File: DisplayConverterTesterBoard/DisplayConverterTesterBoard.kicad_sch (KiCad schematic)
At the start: 1 part

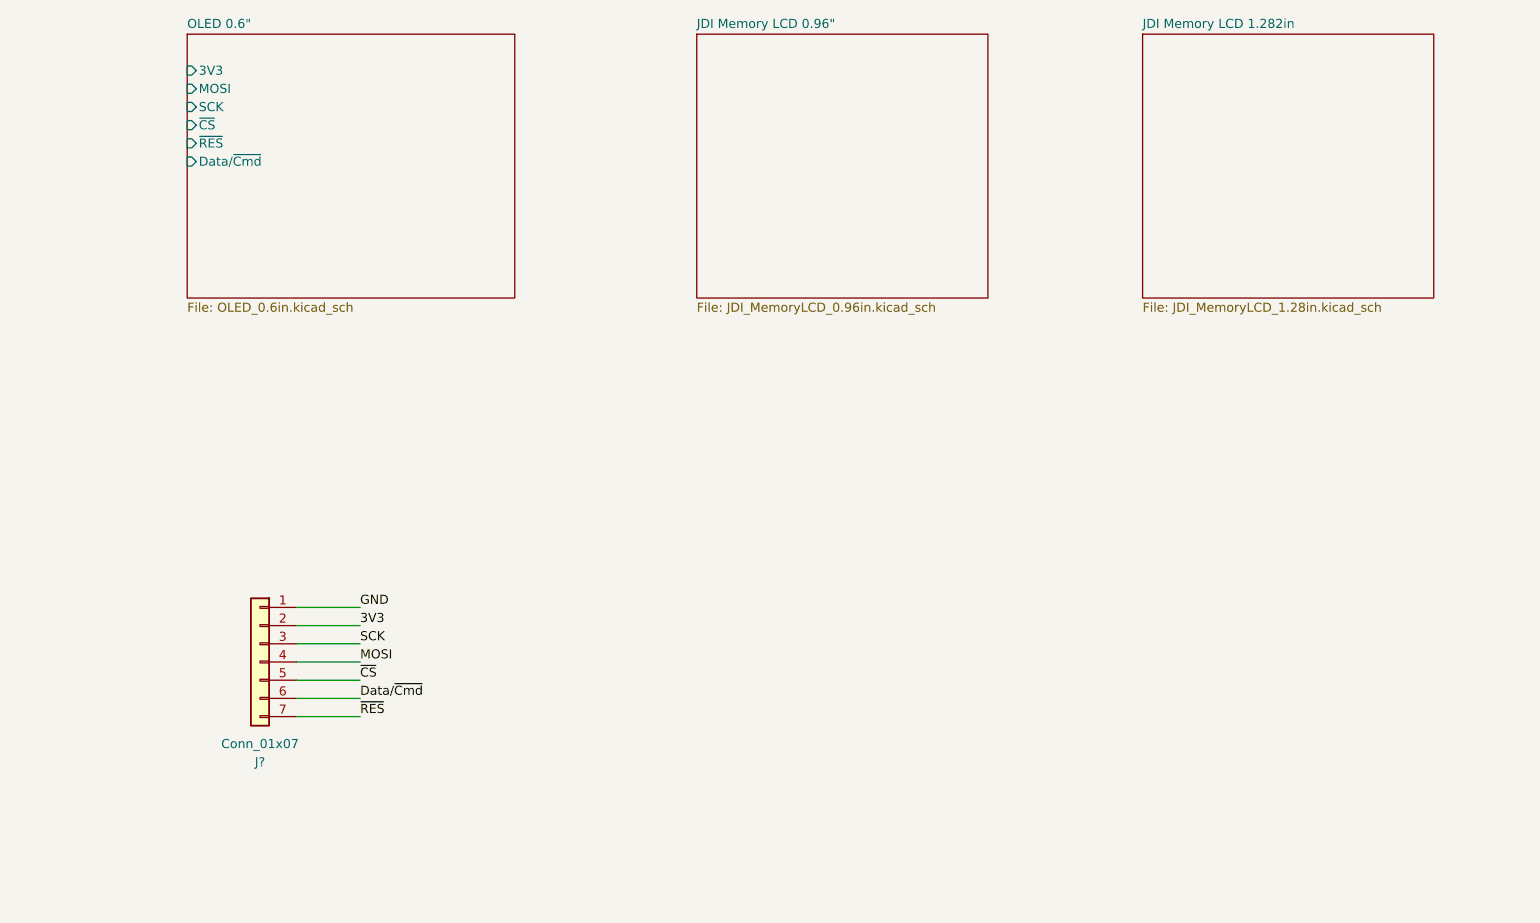
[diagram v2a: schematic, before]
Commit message: fix pinout
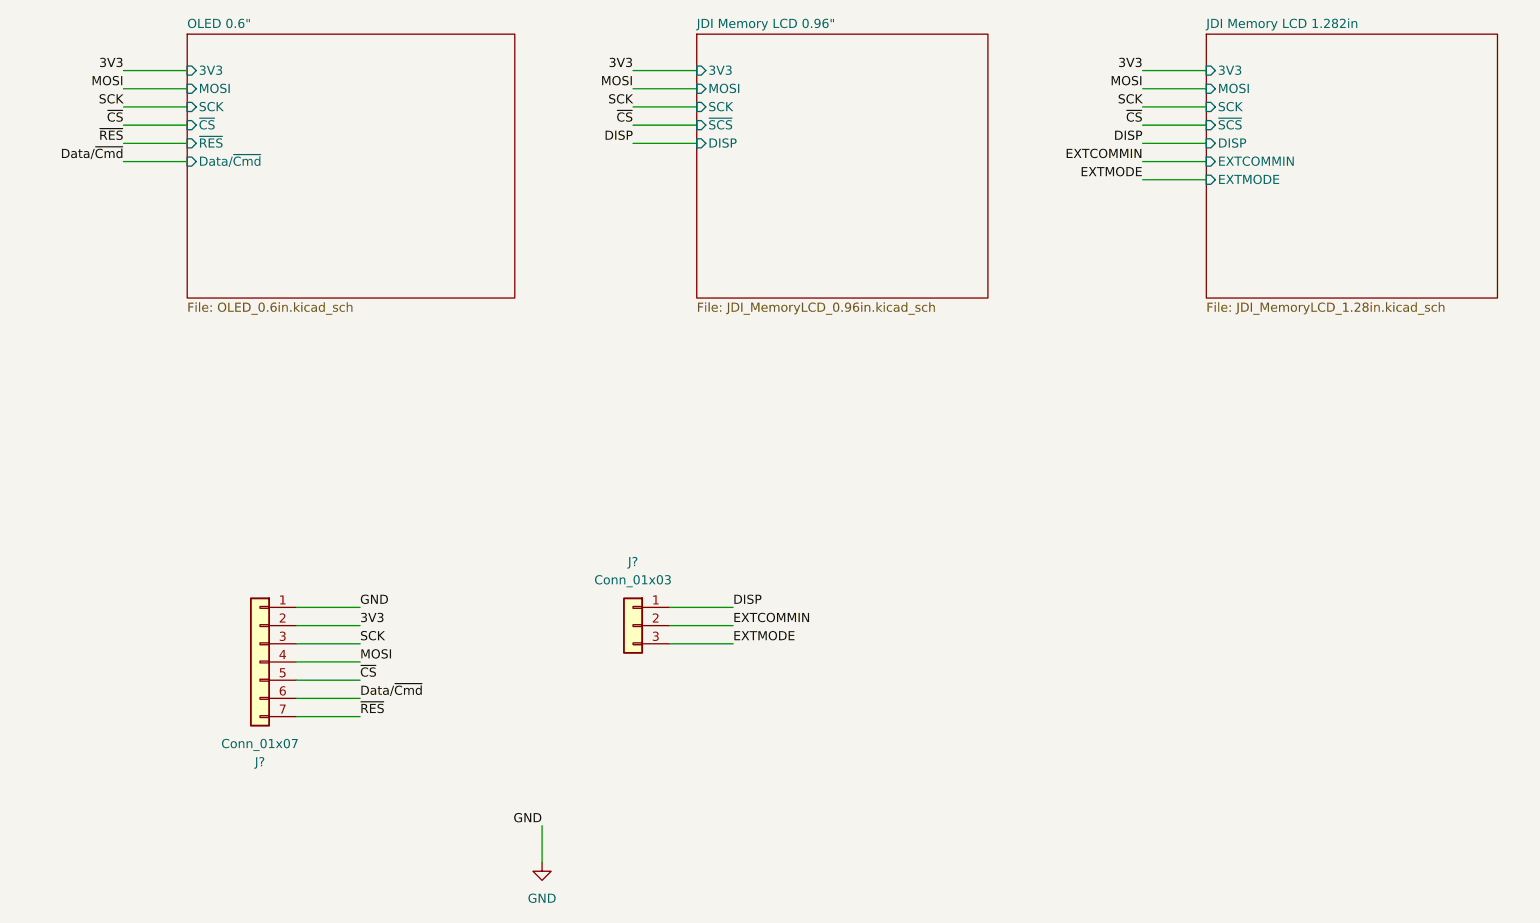
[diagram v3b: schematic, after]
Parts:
- added J?: Conn_01x03, Connector_PinHeader_2.54mm:PinHeader_1x03_P2.54mm_Vertical, symbol Connector_Generic:Conn_01x03
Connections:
- new net DISP: J?.1 (Pin_1)
- new net EXTCOMMIN: J?.2 (Pin_2)
- new net EXTMODE: J?.3 (Pin_3)
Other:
- sheet JDI Memory LCD 0.96" ports: added 3V3, DISP, MOSI, SCK, ~{SCS}; removed none
- sheet JDI Memory LCD 1.282in ports: added 3V3, DISP, EXTCOMMIN, EXTMODE, MOSI, SCK, ~{SCS}; removed none
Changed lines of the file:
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@@
+    (stroke (width 0) (type default))
+  )
+  (wire (pts (xy 120.65 130.81) (xy 129.54 130.81))
+    (stroke (width 0) (type default))
+  )
+  (wire (pts (xy 195.58 58.42) (xy 186.69 58.42))
+    (stroke (width 0) (type default))
+  )
+  (wire (pts (xy 53.34 63.5) (xy 44.45 63.5))
+    (stroke (width 0) (type default))
+  )
+  (wire (pts (xy 195.58 63.5) (xy 186.69 63.5))
+    (stroke (width 0) (type default))
+  )
+  (wire (pts (xy 195.58 66.04) (xy 186.69 66.04))
+    (stroke (width 0) (type default))
+  )
+  (wire (pts (xy 195.58 55.88) (xy 186.69 55.88))
     (stroke (width 0) (type default))
   )
@@
     (stroke (width 0) (type default))
   )
+  (wire (pts (xy 53.34 68.58) (xy 44.45 68.58))
+    (stroke (width 0) (type default))
+  )
+  (wire (pts (xy 195.58 60.96) (xy 186.69 60.96))
+    (stroke (width 0) (type default))
+  )
+  (wire (pts (xy 124.46 66.04) (xy 115.57 66.04))
+    (stroke (width 0) (type default))
+  )
+  (wire (pts (xy 53.34 55.88) (xy 44.45 55.88))
+    (stroke (width 0) (type default))
+  )
+  (wire (pts (xy 53.34 58.42) (xy 44.45 58.42))
+    (stroke (width 0) (type default))
+  )
   (wire (pts (xy 68.58 135.89) (xy 77.47 135.89))
     (stroke (width 0) (type default))
   )
+  (wire (pts (xy 195.58 68.58) (xy 186.69 68.58))
+    (stroke (width 0) (type default))
+  )
   (wire (pts (xy 68.58 146.05) (xy 77.47 146.05))
     (stroke (width 0) (type default))
   )
+  (wire (pts (xy 124.46 63.5) (xy 115.57 63.5))
+    (stroke (width 0) (type default))
+  )
+  (wire (pts (xy 124.46 58.42) (xy 115.57 58.42))
+    (stroke (width 0) (type default))
+  )
   (wire (pts (xy 68.58 140.97) (xy 77.47 140.97))
     (stroke (width 0) (type default))
   )
+  (wire (pts (xy 53.34 66.04) (xy 44.45 66.04))
+    (stroke (width 0) (type default))
+  )
+  (wire (pts (xy 120.65 133.35) (xy 129.54 133.35))
+    (stroke (width 0) (type default))
+  )
+  (wire (pts (xy 195.58 71.12) (xy 186.69 71.12))
+    (stroke (width 0) (type default))
+  )
+  (wire (pts (xy 53.34 60.96) (xy 44.45 60.96))
+    (stroke (width 0) (type default))
+  )
+  (wire (pts (xy 120.65 135.89) (xy 129.54 135.89))
+    (stroke (width 0) (type default))
+  )
+  (wire (pts (xy 124.46 60.96) (xy 115.57 60.96))
+    (stroke (width 0) (type default))
+  )
+  (wire (pts (xy 102.87 161.29) (xy 102.87 166.37))
+    (stroke (width 0) (type default))
+  )
+  (wire (pts (xy 124.46 55.88) (xy 115.57 55.88))
+    (stroke (width 0) (type default))
+  )
+  (label "3V3" (at 115.57 55.88 180) (fields_autoplaced)
+    (effects (font (size 1.27 1.27)) (justify right bottom))
+  )
+  (label "DISP" (at 115.57 66.04 180) (fields_autoplaced)
+    (effects (font (size 1.27 1.27)) (justify right bottom))
+  )
+  (label "EXTCOMMIN" (at 129.54 133.35 0) (fields_autoplaced)
+    (effects (font (size 1.27 1.27)) (justify left bottom))
+  )
   (label "SCK" (at 77.47 135.89 0) (fields_autoplaced)
     (effects (font (size 1.27 1.27)) (justify left bottom))
   )
+  (label "EXTMODE" (at 186.69 71.12 180) (fields_autoplaced)
+    (effects (font (size 1.27 1.27)) (justify right bottom))
+  )
+  (label "GND" (at 102.87 161.29 180) (fields_autoplaced)
+    (effects (font (size 1.27 1.27)) (justify right bottom))
+  )
   (label "MOSI" (at 77.47 138.43 0) (fields_autoplaced)
     (effects (font (size 1.27 1.27)) (justify left bottom))
   )
+  (label "SCK" (at 44.45 60.96 180) (fields_autoplaced)
+    (effects (font (size 1.27 1.27)) (justify right bottom))
+  )
+  (label "MOSI" (at 115.57 58.42 180) (fields_autoplaced)
+    (effects (font (size 1.27 1.27)) (justify right bottom))
+  )
+  (label "EXTCOMMIN" (at 186.69 68.58 180) (fields_autoplaced)
+    (effects (font (size 1.27 1.27)) (justify right bottom))
+  )
+  (label "MOSI" (at 186.69 58.42 180) (fields_autoplaced)
+    (effects (font (size 1.27 1.27)) (justify right bottom))
+  )
+  (label "MOSI" (at 44.45 58.42 180) (fields_autoplaced)
+    (effects (font (size 1.27 1.27)) (justify right bottom))
+  )
+  (label "3V3" (at 44.45 55.88 180) (fields_autoplaced)
+    (effects (font (size 1.27 1.27)) (justify right bottom))
+  )
   (label "Data{slash}~{Cmd}" (at 77.47 143.51 0) (fields_autoplaced)
     (effects (font (size 1.27 1.27)) (justify left bottom))
@@
     (effects (font (size 1.27 1.27)) (justify left bottom))
   )
+  (label "3V3" (at 186.69 55.88 180) (fields_autoplaced)
+    (effects (font (size 1.27 1.27)) (justify right bottom))
+  )
+  (label "~{RES}" (at 44.45 66.04 180) (fields_autoplaced)
+    (effects (font (size 1.27 1.27)) (justify right bottom))
+  )
+  (label "~{CS}" (at 186.69 63.5 180) (fields_autoplaced)
+    (effects (font (size 1.27 1.27)) (justify right bottom))
+  )
+  (label "Data{slash}~{Cmd}" (at 44.45 68.58 180) (fields_autoplaced)
+    (effects (font (size 1.27 1.27)) (justify right bottom))
+  )
+  (label "~{CS}" (at 44.45 63.5 180) (fields_autoplaced)
+    (effects (font (size 1.27 1.27)) (justify right bottom))
+  )
   (label "3V3" (at 77.47 133.35 0) (fields_autoplaced)
     (effects (font (size 1.27 1.27)) (justify left bottom))
   )
+  (label "SCK" (at 186.69 60.96 180) (fields_autoplaced)
+    (effects (font (size 1.27 1.27)) (justify right bottom))
+  )
+  (label "DISP" (at 186.69 66.04 180) (fields_autoplaced)
+    (effects (font (size 1.27 1.27)) (justify right bottom))
+  )
+  (label "EXTMODE" (at 129.54 135.89 0) (fields_autoplaced)
+    (effects (font (size 1.27 1.27)) (justify left bottom))
+  )
+  (label "DISP" (at 129.54 130.81 0) (fields_autoplaced)
+    (effects (font (size 1.27 1.27)) (justify left bottom))
+  )
+  (label "SCK" (at 115.57 60.96 180) (fields_autoplaced)
+    (effects (font (size 1.27 1.27)) (justify right bottom))
+  )
+  (label "~{CS}" (at 115.57 63.5 180) (fields_autoplaced)
+    (effects (font (size 1.27 1.27)) (justify right bottom))
+  )
   (label "GND" (at 77.47 130.81 0) (fields_autoplaced)
     (effects (font (size 1.27 1.27)) (justify left bottom))
@@
   (label "~{RES}" (at 77.47 146.05 0) (fields_autoplaced)
     (effects (font (size 1.27 1.27)) (justify left bottom))
+  )
+  (symbol (lib_id "power:GND") (at 102.87 166.37 0) (unit 1)
+    (in_bom yes) (on_board yes) (dnp no) (fields_autoplaced)
+    (property "Reference" "#PWR0101" (at 102.87 172.72 0)
+      (effects (font (size 1.27 1.27)) hide)
+    )
+    (property "Value" "GND" (at 102.87 171.45 0)
+      (effects (font (size 1.27 1.27)))
+    )
+    (property "Footprint" "" (at 102.87 166.37 0)
+      (effects (font (size 1.27 1.27)) hide)
+    )
+    (property "Datasheet" "" (at 102.87 166.37 0)
+      (effects (font (size 1.27 1.27)) hide)
+    )
+    (pin "1")
+    (instances
+      (project "DisplayConverterTesterBoard"
+        (path "/58d9d6aa-d5e3-4b7b-b546-d57c329de758"
+          (reference "#PWR0101") (unit 1)
+        )
+      )
+    )
   )
   (symbol (lib_id "Connector_Generic:Conn_01x07") (at 63.5 138.43 0) (mirror y) (unit 1)
@@
     )
   )
-  (sheet (at 186.69 50.8) (size 40.64 36.83) (fields_autoplaced)
+  (symbol (lib_id "Connector_Generic:Conn_01x03") (at 115.57 133.35 0) (mirror y) (unit 1)
+    (in_bom yes) (on_board yes) (dnp no) (fields_autoplaced)
+    (property "Reference" "J?" (at 115.57 124.46 0)
+      (effects (font (size 1.27 1.27)))
+    )
+    (property "Value" "Conn_01x03" (at 115.57 127 0)
+      (effects (font (size 1.27 1.27)))
+    )
+    (property "Footprint" "Connector_PinHeader_2.54mm:PinHeader_1x03_P2.54mm_Vertical" (at 115.57 133.35 0)
+      (effects (font (size 1.27 1.27)) hide)
+    )
+    (property "Datasheet" "~" (at 115.57 133.35 0)
+      (effects (font (size 1.27 1.27)) hide)
+    )
+    (pin "1")
+    (pin "2")
+    (pin "3")
+    (instances
+      (project "DisplayConverterTesterBoard"
+        (path "/58d9d6aa-d5e3-4b7b-b546-d57c329de758"
+          (reference "J?") (unit 1)
+        )
+      )
+    )
+  )
+  (sheet (at 195.58 50.8) (size 40.64 36.83) (fields_autoplaced)
     (stroke (width 0.1524) (type solid))
     (fill (color 0 0 0 0.0000))
-    (property "Sheetname" "JDI Memory LCD 1.282in" (at 186.69 50.0884 0)
+    (property "Sheetname" "JDI Memory LCD 1.282in" (at 195.58 50.0884 0)
       (effects (font (size 1.27 1.27)) (justify left bottom))
     )
-    (property "Sheetfile" "JDI_MemoryLCD_1.28in.kicad_sch" (at 186.69 88.2146 0)
+    (property "Sheetfile" "JDI_MemoryLCD_1.28in.kicad_sch" (at 195.58 88.2146 0)
       (effects (font (size 1.27 1.27)) (justify left top))
+    )
+    (pin "MOSI" input (at 195.58 58.42 180)
+      (effects (font (size 1.27 1.27)) (justify left))
+    )
+    (pin "DISP" input (at 195.58 66.04 180)
+      (effects (font (size 1.27 1.27)) (justify left))
+    )
+    (pin "~{SCS}" input (at 195.58 63.5 180)
+      (effects (font (size 1.27 1.27)) (justify left))
+    )
+    (pin "3V3" input (at 195.58 55.88 180)
+      (effects (font (size 1.27 1.27)) (justify left))
+    )
+    (pin "SCK" input (at 195.58 60.96 180)
+      (effects (font (size 1.27 1.27)) (justify left))
+    )
+    (pin "EXTCOMMIN" input (at 195.58 68.58 180)
+      (effects (font (size 1.27 1.27)) (justify left))
+    )
+    (pin "EXTMODE" input (at 195.58 71.12 180)
+      (effects (font (size 1.27 1.27)) (justify left))
     )
     (instances
@@
       (effects (font (size 1.27 1.27)) (justify left top))
     )
-    (instances
+    (pin "~{SCS}" input (at 124.46 63.5 180)
+      (effects (font (size 1.27 1.27)) (justify left))
+    )
+    (pin "3V3" input (at 124.46 55.88 180)
+      (effects (font (size 1.27 1.27)) (justify left))
+    )
+    (pin "MOSI" input (at 124.46 58.42 180)
+      (effects (font (size 1.27 1.27)) (justify left))
+    )
+    (pin "SCK" input (at 124.46 60.96 180)
+      (effects (font (size 1.27 1.27)) (justify left))
+    )
+    (pin "DISP" input (at 124.46 66.04 180)
+      (effects (font (size 1.27 1.27)) (justify left))
+    )
+    (instances

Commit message: annotate all components
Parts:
- gave numbers to parts that had none: 1
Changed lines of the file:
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@@
         )
         (path "/58d9d6aa-d5e3-4b7b-b546-d57c329de758"
-          (reference "J?") (unit 1)
+          (reference "J2") (unit 1)
         )
       )
@@
   (symbol (lib_id "Connector_Generic:Conn_01x03") (at 115.57 133.35 0) (mirror y) (unit 1)
     (in_bom yes) (on_board yes) (dnp no) (fields_autoplaced)
-    (property "Reference" "J?" (at 115.57 124.46 0)
+    (property "Reference" "J3" (at 115.57 124.46 0)
       (effects (font (size 1.27 1.27)))
     )
@@
       (project "DisplayConverterTesterBoard"
         (path "/58d9d6aa-d5e3-4b7b-b546-d57c329de758"
-          (reference "J?") (unit 1)
+          (reference "J3") (unit 1)
         )
       )

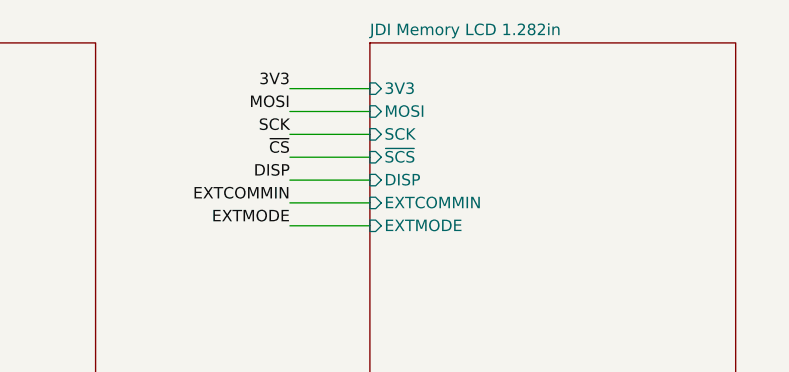
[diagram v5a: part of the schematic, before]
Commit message: updated layout
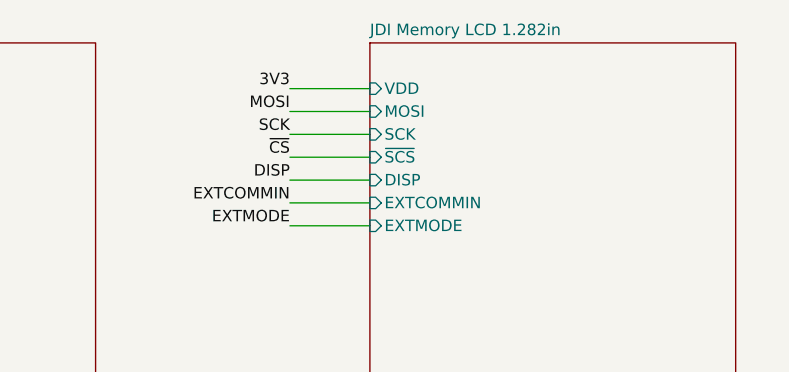
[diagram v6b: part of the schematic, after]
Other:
- sheet JDI Memory LCD 1.282in ports: added VDD; removed 3V3
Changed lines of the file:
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@@
-      (effects (font (size 1.27 1.27)) (justify left))
-    )
-    (pin "3V3" input (at 195.58 55.88 180)
       (effects (font (size 1.27 1.27)) (justify left))
     )
@@
       (effects (font (size 1.27 1.27)) (justify left))
     )
+    (pin "VDD" input (at 195.58 55.88 180)
+      (effects (font (size 1.27 1.27)) (justify left))
+    )
